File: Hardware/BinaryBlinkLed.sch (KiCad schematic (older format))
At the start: 16 parts

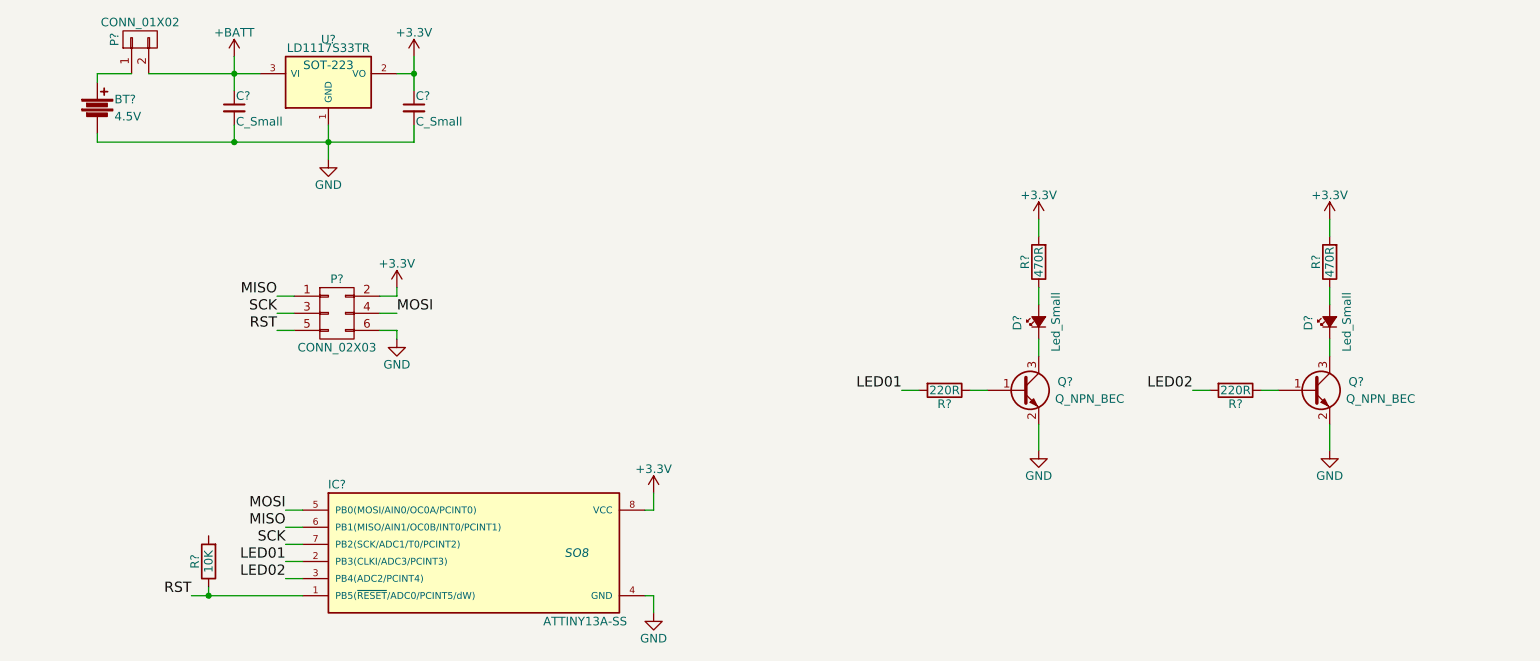
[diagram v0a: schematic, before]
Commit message: Correct value of resistor for supply voltaje 3.3V
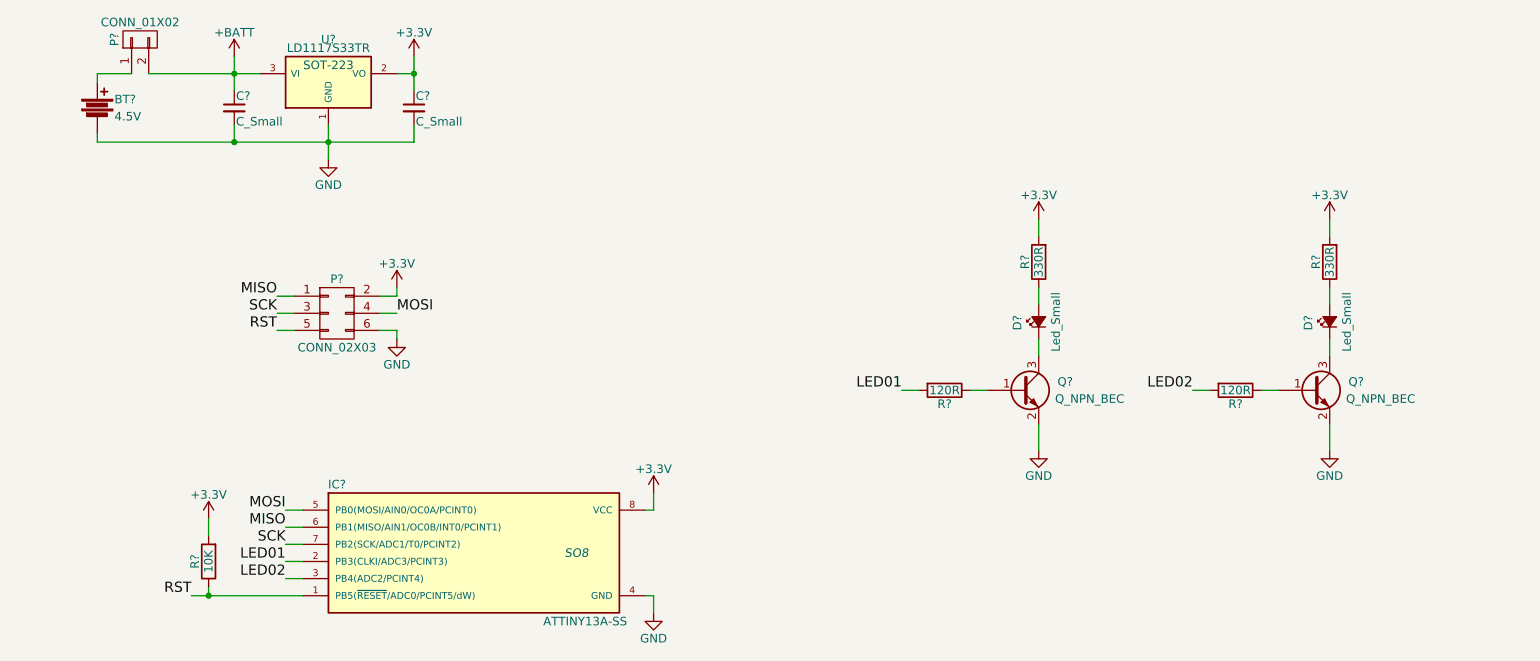
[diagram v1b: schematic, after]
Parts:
- R? (x2): value 220R -> 120R
- R? (x2): value 470R -> 330R
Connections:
- net +3V3: now also R?.2
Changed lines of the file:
@@
 LIBS:contrib
 LIBS:valves
+LIBS:BinaryBlinkLed-cache
 EELAYER 25 0
 EELAYER END
@@
 P 6350 3550
 F 0 "R?" V 6430 3550 50  0000 C CNN
-F 1 "220R" V 6350 3550 50  0000 C CNN
+F 1 "120R" V 6350 3550 50  0000 C CNN
 F 2 "" V 6280 3550 50  0000 C CNN
 F 3 "" H 6350 3550 50  0000 C CNN
@@
 P 6900 2800
 F 0 "R?" V 6980 2800 50  0000 C CNN
-F 1 "470R" V 6900 2800 50  0000 C CNN
+F 1 "330R" V 6900 2800 50  0000 C CNN
 F 2 "" V 6830 2800 50  0000 C CNN
 F 3 "" H 6900 2800 50  0000 C CNN
@@
 P 8050 3550
 F 0 "R?" V 8130 3550 50  0000 C CNN
-F 1 "220R" V 8050 3550 50  0000 C CNN
+F 1 "120R" V 8050 3550 50  0000 C CNN
 F 2 "" V 7980 3550 50  0000 C CNN
 F 3 "" H 8050 3550 50  0000 C CNN
@@
 P 8600 2800
 F 0 "R?" V 8680 2800 50  0000 C CNN
-F 1 "470R" V 8600 2800 50  0000 C CNN
+F 1 "330R" V 8600 2800 50  0000 C CNN
 F 2 "" V 8530 2800 50  0000 C CNN
 F 3 "" H 8600 2800 50  0000 C CNN
@@
 Wire Wire Line
 	6200 3550 6100 3550
+$Comp
+L +3.3V #PWR?
+U 1 1 5945EF5C
+P 2050 4300
+F 0 "#PWR?" H 2050 4150 50  0001 C CNN
+F 1 "+3.3V" H 2050 4440 50  0000 C CNN
+F 2 "" H 2050 4300 50  0000 C CNN
+F 3 "" H 2050 4300 50  0000 C CNN
+	1    2050 4300
+	1    0    0    -1
+$EndComp
+Wire Wire Line
+	2050 4300 2050 4400
 $EndSCHEMATC

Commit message: Remove regulator, set value and name of some components
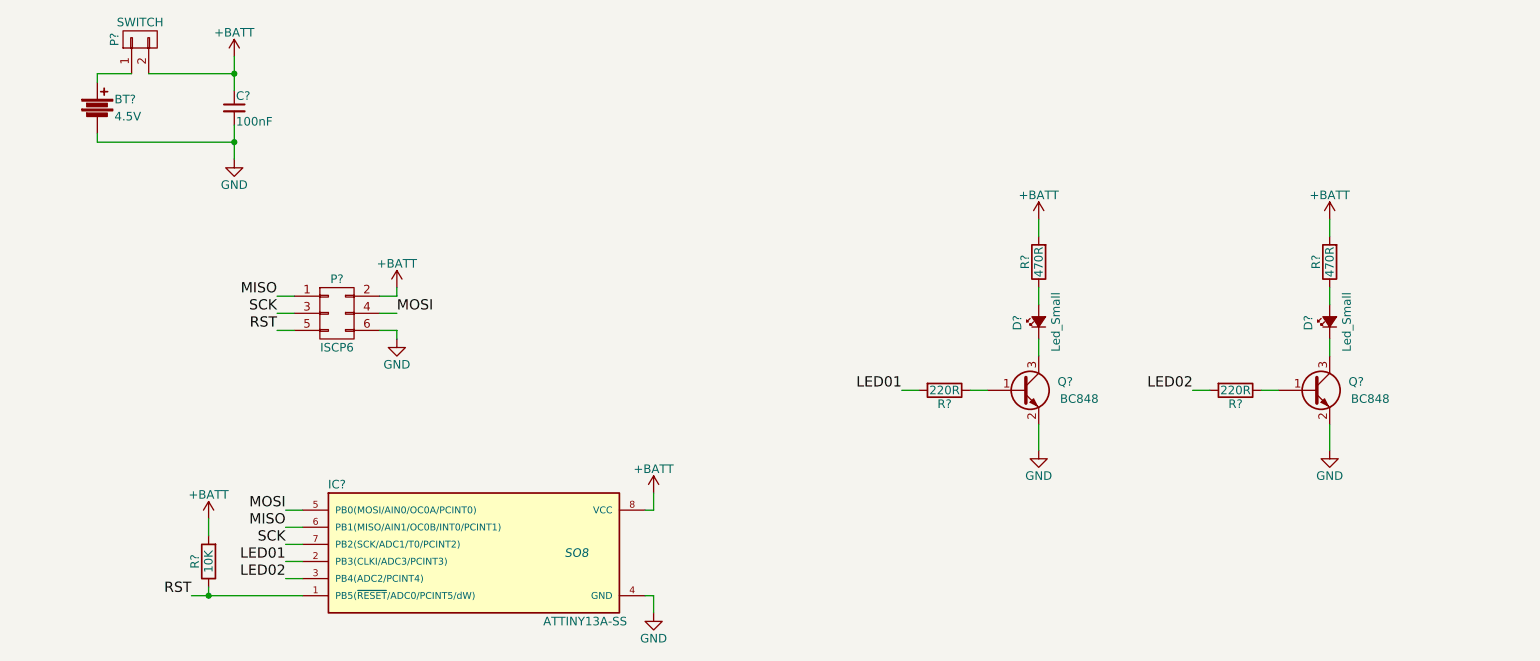
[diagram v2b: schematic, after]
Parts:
- removed C?: C_Small, symbol C_Small
- removed U?: LD1117S33TR, SOT-223, symbol LD1117S33TR
- C?: value C_Small -> 100nF
- P?: value CONN_01X02 -> SWITCH
- P?: value CONN_02X03 -> ISCP6
- Q? (x2): value Q_NPN_BEC -> BC848
- R? (x2): value 120R -> 220R
- R? (x2): value 330R -> 470R
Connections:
- net +3V3 is gone; now on net +BATT: IC?.8 (VCC), P?.2 (P2), R?.2, R?.2, R?.2
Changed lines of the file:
@@
 P 6800 3550
 F 0 "Q?" H 7100 3600 50  0000 R CNN
-F 1 "Q_NPN_BEC" H 7400 3500 50  0000 R CNN
+F 1 "BC848" H 7250 3500 50  0000 R CNN
 F 2 "" H 7000 3650 50  0000 C CNN
 F 3 "" H 6800 3550 50  0000 C CNN
@@
 P 1650 1500
 F 0 "P?" H 1650 1650 50  0000 C CNN
-F 1 "CONN_01X02" V 1750 1500 50  0000 C CNN
+F 1 "SWITCH" V 1750 1500 50  0000 C CNN
 F 2 "" H 1650 1500 50  0000 C CNN
 F 3 "" H 1650 1500 50  0000 C CNN
@@
 P 6350 3550
 F 0 "R?" V 6430 3550 50  0000 C CNN
-F 1 "120R" V 6350 3550 50  0000 C CNN
+F 1 "220R" V 6350 3550 50  0000 C CNN
 F 2 "" V 6280 3550 50  0000 C CNN
 F 3 "" H 6350 3550 50  0000 C CNN
@@
 P 6900 2800
 F 0 "R?" V 6980 2800 50  0000 C CNN
-F 1 "330R" V 6900 2800 50  0000 C CNN
+F 1 "470R" V 6900 2800 50  0000 C CNN
 F 2 "" V 6830 2800 50  0000 C CNN
 F 3 "" H 6900 2800 50  0000 C CNN
@@
 P 8500 3550
 F 0 "Q?" H 8800 3600 50  0000 R CNN
-F 1 "Q_NPN_BEC" H 9100 3500 50  0000 R CNN
+F 1 "BC848" H 8950 3500 50  0000 R CNN
 F 2 "" H 8700 3650 50  0000 C CNN
 F 3 "" H 8500 3550 50  0000 C CNN
@@
 P 8050 3550
 F 0 "R?" V 8130 3550 50  0000 C CNN
-F 1 "120R" V 8050 3550 50  0000 C CNN
+F 1 "220R" V 8050 3550 50  0000 C CNN
 F 2 "" V 7980 3550 50  0000 C CNN
 F 3 "" H 8050 3550 50  0000 C CNN
@@
 P 8600 2800
 F 0 "R?" V 8680 2800 50  0000 C CNN
-F 1 "330R" V 8600 2800 50  0000 C CNN
+F 1 "470R" V 8600 2800 50  0000 C CNN
 F 2 "" V 8530 2800 50  0000 C CNN
 F 3 "" H 8600 2800 50  0000 C CNN
@@
 $EndComp
 $Comp
-L LD1117S33TR U?
-U 1 1 5945F9C8
-P 2750 1750
-F 0 "U?" H 2750 2000 50  0000 C CNN
-F 1 "LD1117S33TR" H 2750 1950 50  0000 C CNN
-F 2 "SOT-223" H 2750 1850 50  0000 C CNN
-F 3 "" H 2750 1750 50  0000 C CNN
-	1    2750 1750
-	1    0    0    -1
-$EndComp
-$Comp
 L C_Small C?
 U 1 1 5945FBCF
 P 2200 1900
 F 0 "C?" H 2210 1970 50  0000 L CNN
-F 1 "C_Small" H 2210 1820 50  0000 L CNN
+F 1 "100nF" H 2210 1820 50  0000 L CNN
 F 2 "" H 2200 1900 50  0000 C CNN
 F 3 "" H 2200 1900 50  0000 C CNN
@@
 	1    0    0    -1
 $EndComp
-$Comp
-L C_Small C?
-U 1 1 5945FC91
-P 3250 1900
-F 0 "C?" H 3260 1970 50  0000 L CNN
-F 1 "C_Small" H 3260 1820 50  0000 L CNN
-F 2 "" H 3250 1900 50  0000 C CNN
-F 3 "" H 3250 1900 50  0000 C CNN
-	1    3250 1900
-	1    0    0    -1
-$EndComp
 Wire Wire Line
 	6500 3550 6600 3550
@@
 Wire Wire Line
 	8600 3750 8600 3900
-Wire Wire Line
-	1700 1700 2350 1700
 Wire Wire Line
 	2200 1600 2200 1800
@@
 Wire Wire Line
 	1600 1700 1400 1700
-$Comp
-L GND #PWR?
-U 1 1 594602D8
-P 2750 2200
-F 0 "#PWR?" H 2750 1950 50  0001 C CNN
-F 1 "GND" H 2750 2050 50  0000 C CNN
-F 2 "" H 2750 2200 50  0000 C CNN
-F 3 "" H 2750 2200 50  0000 C CNN
-	1    2750 2200
-	1    0    0    -1
-$EndComp
 Wire Wire Line
 	1400 2050 1400 2100
 Wire Wire Line
-	1400 2100 3250 2100
-Wire Wire Line
-	2750 2000 2750 2200
-Wire Wire Line
-	2200 2000 2200 2100
+	2200 2000 2200 2200
 Connection ~ 2200 2100
 Wire Wire Line
 	1400 1700 1400 1750
-Connection ~ 2750 2100
-Wire Wire Line
-	3150 1700 3250 1700
-Wire Wire Line
-	3250 1600 3250 1800
-Wire Wire Line
-	3250 2100 3250 2000
-$Comp
-L +3.3V #PWR?
-U 1 1 59460664
-P 3250 1600
-F 0 "#PWR?" H 3250 1450 50  0001 C CNN
-F 1 "+3.3V" H 3250 1740 50  0000 C CNN
-F 2 "" H 3250 1600 50  0000 C CNN
-F 3 "" H 3250 1600 50  0000 C CNN
-	1    3250 1600
-	1    0    0    -1
-$EndComp
-Connection ~ 3250 1700
-$Comp
-L +3.3V #PWR?
-U 1 1 59460820
-P 6900 2550
-F 0 "#PWR?" H 6900 2400 50  0001 C CNN
-F 1 "+3.3V" H 6900 2690 50  0000 C CNN
-F 2 "" H 6900 2550 50  0000 C CNN
-F 3 "" H 6900 2550 50  0000 C CNN
-	1    6900 2550
-	1    0    0    -1
-$EndComp
-$Comp
-L +3.3V #PWR?
-U 1 1 59460A2B
-P 8600 2550
-F 0 "#PWR?" H 8600 2400 50  0001 C CNN
-F 1 "+3.3V" H 8600 2690 50  0000 C CNN
-F 2 "" H 8600 2550 50  0000 C CNN
-F 3 "" H 8600 2550 50  0000 C CNN
-	1    8600 2550
-	1    0    0    -1
-$EndComp
 $Comp
 L CONN_02X03 P?
@@
 P 2800 3100
 F 0 "P?" H 2800 3300 50  0000 C CNN
-F 1 "CONN_02X03" H 2800 2900 50  0000 C CNN
+F 1 "ISCP6" H 2800 2900 50  0000 C CNN
 F 2 "" H 2800 1900 50  0000 C CNN
 F 3 "" H 2800 1900 50  0000 C CNN
@@
 	1    0    0    -1
 $EndComp
-$Comp
-L +3.3V #PWR?
-U 1 1 59461649
-P 3150 2950
-F 0 "#PWR?" H 3150 2800 50  0001 C CNN
-F 1 "+3.3V" H 3150 3090 50  0000 C CNN
-F 2 "" H 3150 2950 50  0000 C CNN
-F 3 "" H 3150 2950 50  0000 C CNN
-	1    3150 2950
-	1    0    0    -1
-$EndComp
 Wire Wire Line
 	3150 3000 3150 2950
@@
 RST
 Connection ~ 2050 4750
-$Comp
-L +3.3V #PWR?
-U 1 1 5946223D
-P 4650 4150
-F 0 "#PWR?" H 4650 4000 50  0001 C CNN
-F 1 "+3.3V" H 4650 4290 50  0000 C CNN
-F 2 "" H 4650 4150 50  0000 C CNN
-F 3 "" H 4650 4150 50  0000 C CNN
-	1    4650 4150
-	1    0    0    -1
-$EndComp
 $Comp
 L GND #PWR?
@@
 Wire Wire Line
 	6200 3550 6100 3550
-$Comp
-L +3.3V #PWR?
-U 1 1 5945EF5C
+Wire Wire Line
+	2050 4300 2050 4400
+$Comp
+L GND #PWR?
+U 1 1 5946369E
+P 2200 2200
+F 0 "#PWR?" H 2200 1950 50  0001 C CNN
+F 1 "GND" H 2200 2050 50  0000 C CNN
+F 2 "" H 2200 2200 50  0000 C CNN
+F 3 "" H 2200 2200 50  0000 C CNN
+	1    2200 2200
+	1    0    0    -1
+$EndComp
+Wire Wire Line
+	1400 2100 2200 2100
+Wire Wire Line
+	1700 1700 2200 1700
+$Comp
+L +BATT #PWR?
+U 1 1 59463F9B
+P 3150 2950
+F 0 "#PWR?" H 3150 2800 50  0001 C CNN
+F 1 "+BATT" H 3150 3090 50  0000 C CNN
+F 2 "" H 3150 2950 50  0000 C CNN
+F 3 "" H 3150 2950 50  0000 C CNN
+	1    3150 2950
+	1    0    0    -1
+$EndComp
+$Comp
+L +BATT #PWR?
+U 1 1 594640CC
 P 2050 4300
 F 0 "#PWR?" H 2050 4150 50  0001 C CNN
-F 1 "+3.3V" H 2050 4440 50  0000 C CNN
+F 1 "+BATT" H 2050 4440 50  0000 C CNN
 F 2 "" H 2050 4300 50  0000 C CNN
 F 3 "" H 2050 4300 50  0000 C CNN
@@
 	1    0    0    -1
 $EndComp
-Wire Wire Line
-	2050 4300 2050 4400
+$Comp
+L +BATT #PWR?
+U 1 1 5946412B
+P 6900 2550
+F 0 "#PWR?" H 6900 2400 50  0001 C CNN
+F 1 "+BATT" H 6900 2690 50  0000 C CNN
+F 2 "" H 6900 2550 50  0000 C CNN
+F 3 "" H 6900 2550 50  0000 C CNN
+	1    6900 2550
+	1    0    0    -1
+$EndComp
+$Comp
+L +BATT #PWR?
+U 1 1 59464198
+P 8600 2550
+F 0 "#PWR?" H 8600 2400 50  0001 C CNN
+F 1 "+BATT" H 8600 2690 50  0000 C CNN
+F 2 "" H 8600 2550 50  0000 C CNN
+F 3 "" H 8600 2550 50  0000 C CNN
+	1    8600 2550
+	1    0    0    -1
+$EndComp
+$Comp
+L +BATT #PWR?
+U 1 1 5946424C
+P 4650 4150
+F 0 "#PWR?" H 4650 4000 50  0001 C CNN
+F 1 "+BATT" H 4650 4290 50  0000 C CNN
+F 2 "" H 4650 4150 50  0000 C CNN
+F 3 "" H 4650 4150 50  0000 C CNN
+	1    4650 4150
+	1    0    0    -1
+$EndComp
 $EndSCHEMATC

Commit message: select packages of components
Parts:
- BT1: renamed from BT?; footprint (none) -> Connect:bornier2
- C1: renamed from C?; footprint (none) -> Capacitors_SMD:C_0805
- D1: renamed from D?; value Led_Small -> Led_01; footprint (none) -> w_smd_leds:Led_1206
- D2: renamed from D?; value Led_Small -> Led_02; footprint (none) -> w_smd_leds:Led_1206
- IC1: renamed from IC?; footprint SO8 -> w_smd_dil:so-8
- P1: renamed from P?; footprint (none) -> w_switch:switch_mmp122-r
- P2: renamed from P?; footprint (none) -> Pin_Headers:Pin_Header_Straight_2x03
- Q1, Q2: renamed from Q?; footprint (none) -> TO_SOT_Packages_SMD:SOT-23
- R1, R2, R3, R4, R5: renamed from R?; footprint (none) -> Resistors_SMD:R_0805
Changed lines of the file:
@@
 $EndDescr
 $Comp
-L ATTINY13A-SS IC?
+L ATTINY13A-SS IC1
 U 1 1 5945DFF3
 P 3600 4500
-F 0 "IC?" H 2800 4900 50  0000 C CNN
+F 0 "IC1" H 2800 4900 50  0000 C CNN
 F 1 "ATTINY13A-SS" H 4250 4100 50  0000 C CNN
-F 2 "SO8" H 4200 4500 50  0000 C CIN
+F 2 "w_smd_dil:so-8" H 4200 4500 50  0000 C CIN
 F 3 "" H 2800 4850 50  0000 C CNN
 	1    3600 4500
@@
 $EndComp
 $Comp
-L Q_NPN_BEC Q?
+L Q_NPN_BEC Q1
 U 1 1 5945E104
 P 6800 3550
-F 0 "Q?" H 7100 3600 50  0000 R CNN
+F 0 "Q1" H 7100 3600 50  0000 R CNN
 F 1 "BC848" H 7250 3500 50  0000 R CNN
-F 2 "" H 7000 3650 50  0000 C CNN
+F 2 "TO_SOT_Packages_SMD:SOT-23" H 7000 3650 50  0001 C CNN
 F 3 "" H 6800 3550 50  0000 C CNN
 	1    6800 3550
@@
 $EndComp
 $Comp
-L Battery BT?
+L Battery BT1
 U 1 1 5945E297
 P 1400 1900
-F 0 "BT?" H 1500 1950 50  0000 L CNN
+F 0 "BT1" H 1500 1950 50  0000 L CNN
 F 1 "4.5V" H 1500 1850 50  0000 L CNN
-F 2 "" V 1400 1940 50  0000 C CNN
+F 2 "Connect:bornier2" V 1400 1940 50  0001 C CNN
 F 3 "" V 1400 1940 50  0000 C CNN
 	1    1400 1900
@@
 $EndComp
 $Comp
-L +BATT #PWR?
+L +BATT #PWR01
 U 1 1 5945E2F7
 P 2200 1600
-F 0 "#PWR?" H 2200 1450 50  0001 C CNN
+F 0 "#PWR01" H 2200 1450 50  0001 C CNN
 F 1 "+BATT" H 2200 1740 50  0000 C CNN
 F 2 "" H 2200 1600 50  0000 C CNN
@@
 $EndComp
 $Comp
-L CONN_01X02 P?
+L CONN_01X02 P1
 U 1 1 5945E36F
 P 1650 1500
-F 0 "P?" H 1650 1650 50  0000 C CNN
+F 0 "P1" H 1650 1650 50  0000 C CNN
 F 1 "SWITCH" V 1750 1500 50  0000 C CNN
-F 2 "" H 1650 1500 50  0000 C CNN
+F 2 "w_switch:switch_mmp122-r" H 1650 1500 50  0001 C CNN
 F 3 "" H 1650 1500 50  0000 C CNN
 	1    1650 1500
@@
 $EndComp
 $Comp
-L R R?
+L R R2
 U 1 1 5945E3F0
 P 6350 3550
-F 0 "R?" V 6430 3550 50  0000 C CNN
+F 0 "R2" V 6430 3550 50  0000 C CNN
 F 1 "220R" V 6350 3550 50  0000 C CNN
-F 2 "" V 6280 3550 50  0000 C CNN
+F 2 "Resistors_SMD:R_0805" V 6280 3550 50  0001 C CNN
 F 3 "" H 6350 3550 50  0000 C CNN
 	1    6350 3550
@@
 $EndComp
 $Comp
-L Led_Small D?
+L Led_Small D1
 U 1 1 5945E6AE
 P 6900 3150
-F 0 "D?" H 6850 3275 50  0000 L CNN
-F 1 "Led_Small" H 6725 3050 50  0000 L CNN
-F 2 "" V 6900 3150 50  0000 C CNN
+F 0 "D1" H 6850 3275 50  0000 L CNN
+F 1 "Led_01" H 6725 3050 50  0000 L CNN
+F 2 "w_smd_leds:Led_1206" V 6900 3150 50  0001 C CNN
 F 3 "" V 6900 3150 50  0000 C CNN
 	1    6900 3150
@@
 $EndComp
 $Comp
-L GND #PWR?
+L GND #PWR02
 U 1 1 5945F10B
 P 6900 3900
-F 0 "#PWR?" H 6900 3650 50  0001 C CNN
+F 0 "#PWR02" H 6900 3650 50  0001 C CNN
 F 1 "GND" H 6900 3750 50  0000 C CNN
 F 2 "" H 6900 3900 50  0000 C CNN
@@
 $EndComp
 $Comp
-L R R?
+L R R3
 U 1 1 5945E4BE
 P 6900 2800
-F 0 "R?" V 6980 2800 50  0000 C CNN
+F 0 "R3" V 6980 2800 50  0000 C CNN
 F 1 "470R" V 6900 2800 50  0000 C CNN
-F 2 "" V 6830 2800 50  0000 C CNN
+F 2 "Resistors_SMD:R_0805" V 6830 2800 50  0001 C CNN
 F 3 "" H 6900 2800 50  0000 C CNN
 	1    6900 2800
@@
 $EndComp
 $Comp
-L Q_NPN_BEC Q?
+L Q_NPN_BEC Q2
 U 1 1 5945F66C
 P 8500 3550
-F 0 "Q?" H 8800 3600 50  0000 R CNN
+F 0 "Q2" H 8800 3600 50  0000 R CNN
 F 1 "BC848" H 8950 3500 50  0000 R CNN
-F 2 "" H 8700 3650 50  0000 C CNN
+F 2 "TO_SOT_Packages_SMD:SOT-23" H 8700 3650 50  0001 C CNN
 F 3 "" H 8500 3550 50  0000 C CNN
 	1    8500 3550
@@
 $EndComp
 $Comp
-L R R?
+L R R4
 U 1 1 5945F672
 P 8050 3550
-F 0 "R?" V 8130 3550 50  0000 C CNN
+F 0 "R4" V 8130 3550 50  0000 C CNN
 F 1 "220R" V 8050 3550 50  0000 C CNN
-F 2 "" V 7980 3550 50  0000 C CNN
+F 2 "Resistors_SMD:R_0805" V 7980 3550 50  0001 C CNN
 F 3 "" H 8050 3550 50  0000 C CNN
 	1    8050 3550
@@
 $EndComp
 $Comp
-L Led_Small D?
+L Led_Small D2
 U 1 1 5945F678
 P 8600 3150
-F 0 "D?" H 8550 3275 50  0000 L CNN
-F 1 "Led_Small" H 8425 3050 50  0000 L CNN
-F 2 "" V 8600 3150 50  0000 C CNN
+F 0 "D2" H 8550 3275 50  0000 L CNN
+F 1 "Led_02" H 8425 3050 50  0000 L CNN
+F 2 "w_smd_leds:Led_1206" V 8600 3150 50  0001 C CNN
 F 3 "" V 8600 3150 50  0000 C CNN
 	1    8600 3150
@@
 $EndComp
 $Comp
-L GND #PWR?
+L GND #PWR03
 U 1 1 5945F684
 P 8600 3900
-F 0 "#PWR?" H 8600 3650 50  0001 C CNN
+F 0 "#PWR03" H 8600 3650 50  0001 C CNN
 F 1 "GND" H 8600 3750 50  0000 C CNN
 F 2 "" H 8600 3900 50  0000 C CNN
@@
 $EndComp
 $Comp
-L R R?
+L R R5
 U 1 1 5945F68A
 P 8600 2800
-F 0 "R?" V 8680 2800 50  0000 C CNN
+F 0 "R5" V 8680 2800 50  0000 C CNN
 F 1 "470R" V 8600 2800 50  0000 C CNN
-F 2 "" V 8530 2800 50  0000 C CNN
+F 2 "Resistors_SMD:R_0805" V 8530 2800 50  0001 C CNN
 F 3 "" H 8600 2800 50  0000 C CNN
 	1    8600 2800
@@
 $EndComp
 $Comp
-L C_Small C?
+L C_Small C1
 U 1 1 5945FBCF
 P 2200 1900
-F 0 "C?" H 2210 1970 50  0000 L CNN
+F 0 "C1" H 2210 1970 50  0000 L CNN
 F 1 "100nF" H 2210 1820 50  0000 L CNN
-F 2 "" H 2200 1900 50  0000 C CNN
+F 2 "Capacitors_SMD:C_0805" H 2200 1900 50  0001 C CNN
 F 3 "" H 2200 1900 50  0000 C CNN
 	1    2200 1900
@@
 	1400 1700 1400 1750
 $Comp
-L CONN_02X03 P?
+L CONN_02X03 P2
 U 1 1 59461245
 P 2800 3100
-F 0 "P?" H 2800 3300 50  0000 C CNN
+F 0 "P2" H 2800 3300 50  0000 C CNN
 F 1 "ISCP6" H 2800 2900 50  0000 C CNN
-F 2 "" H 2800 1900 50  0000 C CNN
+F 2 "Pin_Headers:Pin_Header_Straight_2x03" H 2800 1900 50  0001 C CNN
 F 3 "" H 2800 1900 50  0000 C CNN
 	1    2800 3100
@@
 RST
 $Comp
-L GND #PWR?
+L GND #PWR04
 U 1 1 5946156C
 P 3150 3250
-F 0 "#PWR?" H 3150 3000 50  0001 C CNN
+F 0 "#PWR04" H 3150 3000 50  0001 C CNN
 F 1 "GND" H 3150 3100 50  0000 C CNN
 F 2 "" H 3150 3250 50  0000 C CNN
@@
 	2600 4650 2500 4650
 $Comp
-L R R?
+L R R1
 U 1 1 59461F21
 P 2050 4550
-F 0 "R?" V 2130 4550 50  0000 C CNN
+F 0 "R1" V 2130 4550 50  0000 C CNN
 F 1 "10K" V 2050 4550 50  0000 C CNN
-F 2 "" V 1980 4550 50  0000 C CNN
+F 2 "Resistors_SMD:R_0805" V 1980 4550 50  0001 C CNN
 F 3 "" H 2050 4550 50  0000 C CNN
 	1    2050 4550
@@
 Connection ~ 2050 4750
 $Comp
-L GND #PWR?
+L GND #PWR05
 U 1 1 59462298
 P 4650 4850
-F 0 "#PWR?" H 4650 4600 50  0001 C CNN
+F 0 "#PWR05" H 4650 4600 50  0001 C CNN
 F 1 "GND" H 4650 4700 50  0000 C CNN
 F 2 "" H 4650 4850 50  0000 C CNN
@@
 	2050 4300 2050 4400
 $Comp
-L GND #PWR?
+L GND #PWR06
 U 1 1 5946369E
 P 2200 2200
-F 0 "#PWR?" H 2200 1950 50  0001 C CNN
+F 0 "#PWR06" H 2200 1950 50  0001 C CNN
 F 1 "GND" H 2200 2050 50  0000 C CNN
 F 2 "" H 2200 2200 50  0000 C CNN
@@
 	1700 1700 2200 1700
 $Comp
-L +BATT #PWR?
+L +BATT #PWR07
 U 1 1 59463F9B
 P 3150 2950
-F 0 "#PWR?" H 3150 2800 50  0001 C CNN
+F 0 "#PWR07" H 3150 2800 50  0001 C CNN
 F 1 "+BATT" H 3150 3090 50  0000 C CNN
 F 2 "" H 3150 2950 50  0000 C CNN
@@
 $EndComp
 $Comp
-L +BATT #PWR?
+L +BATT #PWR08
 U 1 1 594640CC
 P 2050 4300
-F 0 "#PWR?" H 2050 4150 50  0001 C CNN
+F 0 "#PWR08" H 2050 4150 50  0001 C CNN
 F 1 "+BATT" H 2050 4440 50  0000 C CNN
 F 2 "" H 2050 4300 50  0000 C CNN
@@
 $EndComp
 $Comp
-L +BATT #PWR?
+L +BATT #PWR09
 U 1 1 5946412B
 P 6900 2550
-F 0 "#PWR?" H 6900 2400 50  0001 C CNN
+F 0 "#PWR09" H 6900 2400 50  0001 C CNN
 F 1 "+BATT" H 6900 2690 50  0000 C CNN
 F 2 "" H 6900 2550 50  0000 C CNN
@@
 $EndComp
 $Comp
-L +BATT #PWR?
+L +BATT #PWR010
 U 1 1 59464198
 P 8600 2550
-F 0 "#PWR?" H 8600 2400 50  0001 C CNN
+F 0 "#PWR010" H 8600 2400 50  0001 C CNN
 F 1 "+BATT" H 8600 2690 50  0000 C CNN
 F 2 "" H 8600 2550 50  0000 C CNN
@@
 $EndComp
 $Comp
-L +BATT #PWR?
+L +BATT #PWR011
 U 1 1 5946424C
 P 4650 4150
-F 0 "#PWR?" H 4650 4000 50  0001 C CNN
+F 0 "#PWR011" H 4650 4000 50  0001 C CNN
 F 1 "+BATT" H 4650 4290 50  0000 C CNN
 F 2 "" H 4650 4150 50  0000 C CNN
